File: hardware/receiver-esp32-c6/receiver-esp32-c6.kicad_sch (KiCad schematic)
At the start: 34 parts, among them J1 Conn_01x04, J2 Conn_01x04, J3 Conn_01x04, J4 Conn_01x06, J5 Conn_01x06, J6 Conn_01x02, J7 Conn_02x04_Counter_Clockwise, J8 Conn_02x03_Counter_Clockwise, J9 Conn_02x02_Counter_Clockwise, SW1 SW_Push_DPDT, U1 ESP32-C6-WROOM-1, U2 ULN2003, U3 MT3608, U4 MT3608

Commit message: First production version - with issues
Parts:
- removed J1, J2, J3: Conn_01x04, symbol Connector_Generic:Conn_01x04
- removed J9: Conn_02x02_Counter_Clockwise, symbol Connector_Generic:Conn_02x02_Counter_Clockwise
- added H1, H2, H3, H4: MountingHole, MountingHole:MountingHole_4mm_Pad_TopBottom, symbol Mechanical:MountingHole
- added J1, J11, J2, J3: Conn_01x03, Connector_PinHeader_2.54mm:PinHeader_1x03_P2.54mm_Vertical, symbol Connector_Generic:Conn_01x03
- added J10, J9: Conn_01x04, Connector_PinHeader_2.54mm:PinHeader_1x04_P2.54mm_Vertical, symbol Connector_Generic:Conn_01x04
- added R10, R11, R13, R14: 10kR 1%, Resistor_SMD:R_0603_1608Metric, symbol Device:R_US
- added R12: ???, Resistor_SMD:R_0805_2012Metric, symbol Device:R_US
- added SW2: SW_Push, Button_Switch_SMD:SW_SPST_PTS647_Sx38, symbol Switch:SW_Push
- added U5: INA226, Package_SO:VSSOP-10_3x3mm_P0.5mm, symbol Sensor_Energy:INA226
- C1, C2, C6, C7, C8, C9: footprint (none) -> Capacitor_SMD:C_0603_1608Metric
- D1, D4: footprint (none) -> Diode_SMD:D_SMF
- D3: footprint (none) -> LED_SMD:LED_0603_1608Metric
- J4, J5: footprint (none) -> Connector_PinHeader_2.54mm:PinHeader_1x06_P2.54mm_Vertical
- J6: footprint (none) -> Connector_JST:JST_EH_B2B-EH-A_1x02_P2.50mm_Vertical
- J7: footprint (none) -> Connector_IDC:IDC-Header_2x04_P2.54mm_Vertical
- J8: footprint (none) -> Connector_PinHeader_1.27mm:PinHeader_2x03_P1.27mm_Vertical_SMD
- L1, L2: footprint (none) -> Inductor_SMD:L_Changjiang_FNR5020S
- R1, R2, R3, R4, R5, R6, R7, R8, R9: footprint (none) -> Resistor_SMD:R_0603_1608Metric
- SW1: footprint (none) -> Minatel Library:Switch-6P-2way
- U2: footprint (none) -> Package_SO:SOP-16_3.9x9.9mm_P1.27mm
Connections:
- net +3V3: now also U1.2 (3V3), J9.1 (Pin_1), R10.2, R11.2, R13.1, R14.1, U5.6 (VS)
- net +5V: now also J1.2 (Pin_2), J11.2 (Pin_2), J2.2 (Pin_2), J3.2 (Pin_2)
- net BOOT: now also R14.2, SW2.2
- net GND: now also J1.3 (Pin_3), J10.4 (Pin_4), J11.3 (Pin_3), J2.3 (Pin_3), J3.3 (Pin_3), J9.4 (Pin_4), SW2.1, U5.1 (A1), U5.2 (A0), U5.7 (GND)
- net I2C_SCL: now also J9.2 (Pin_2), R11.1, U5.5 (SCL)
- net I2C_SDA: now also J9.3 (Pin_3), R10.1, U5.4 (SDA)
- net O_LED_1: now also U1.21 (GPIO23); no longer U1.16 (GPIO18)
- net O_LED_2: now also U1.20 (GPIO22); no longer U1.17 (GPIO19)
- net O_LED_3: now also U1.19 (GPIO21); no longer U1.18 (GPIO20)
- net O_LED_4: now also U1.18 (GPIO20); no longer U1.19 (GPIO21)
- net O_LED_5: now also U1.17 (GPIO19); no longer U1.20 (GPIO22)
- net O_LED_6: now also U1.16 (GPIO18); no longer U1.21 (GPIO23)
- net O_PWM_1: now also J1.1 (Pin_1)
- net O_PWM_2: now also J2.1 (Pin_1)
- net O_PWM_3: now also J3.1 (Pin_1)
- net O_PWM_4: now also J11.1 (Pin_1)
- net O_STEPPER_MS1: now also U1.23 (GPIO15)
- net USB_D+: now also J10.3 (Pin_3)
- net USB_D-: now also J10.2 (Pin_2)
- net VCC: now also J10.1 (Pin_1), R12.2, U5.9 (Vin-); no longer SW1.1 (A)
- net 3V3C: now reaches D4.2 (A), L2.2, U4.1 (SW)
- net 5VC: now reaches D1.2 (A), L1.2, U3.1 (SW)
- net VSS: now reaches SW1.4 (A)
- net VSS: now also SW1.1 (A), R12.1, U5.10 (Vin+), U5.8 (Vbus)
- new net: R13.2, U5.3 (~{Alert})
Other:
- company: (none) -> Pedro Minatel
- title: (none) -> ESP32-C6 ESP-NOW Receiver
- moved on the sheet: C8, C9, D3, J4, J5, J6, R3, R4, R9, SW1, U1, U2

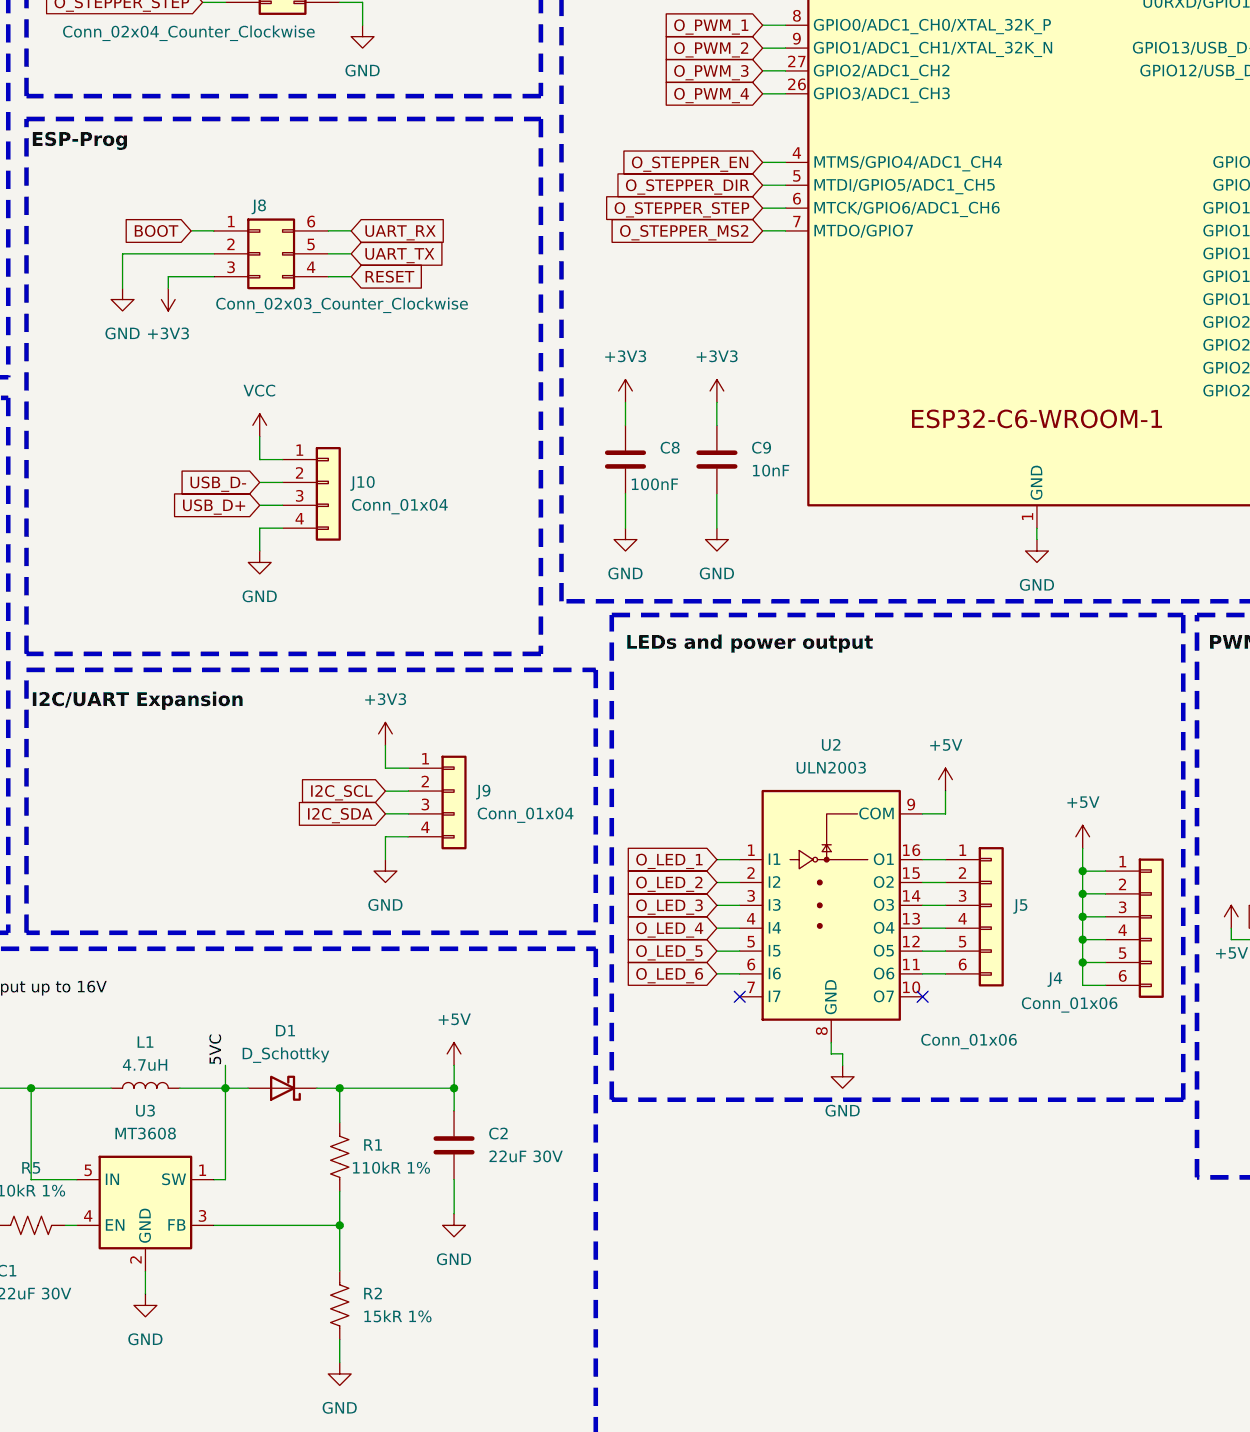
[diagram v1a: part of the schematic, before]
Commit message: Fixed the ESP-PROG pinout
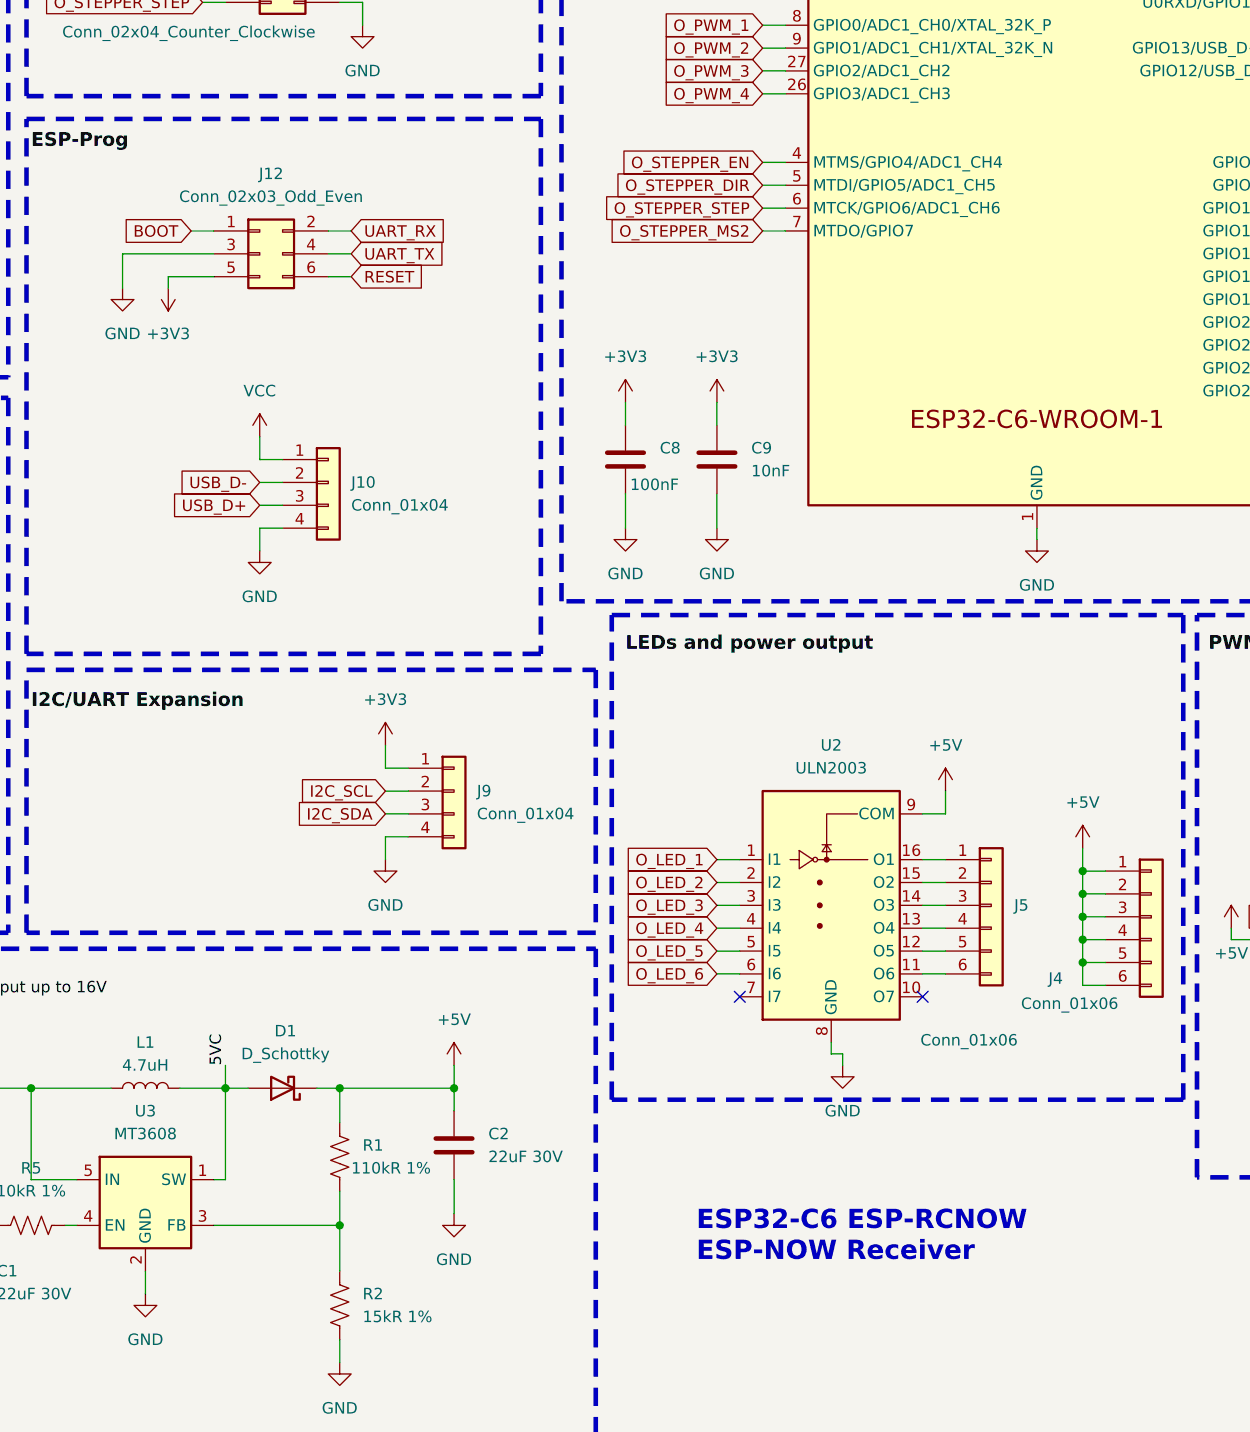
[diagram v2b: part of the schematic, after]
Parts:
- removed J8: Conn_02x03_Counter_Clockwise, Connector_PinHeader_1.27mm:PinHeader_2x03_P1.27mm_Vertical_SMD, symbol Connector_Generic:Conn_02x03_Counter_Clockwise
- added J12: Conn_02x03_Odd_Even, Connector_PinHeader_1.27mm:PinHeader_2x03_P1.27mm_Vertical_SMD, symbol Connector_Generic:Conn_02x03_Odd_Even
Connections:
- net +3V3: now also J12.5 (Pin_5)
- net BOOT: now also J12.1 (Pin_1)
- net GND: now also J12.3 (Pin_3)
- net RESET: now also J12.6 (Pin_6)
- net UART_RX: now also J12.2 (Pin_2)
- net UART_TX: now also J12.4 (Pin_4)
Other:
- note added: "ESP32-C6 ESP-RCNOW ESP-NOW Receiver"
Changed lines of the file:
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@@
 	(title_block
 		(title "ESP32-C6 ESP-NOW Receiver")
-		(date "2025-02-08")
-		(rev "1.0")
+		(date "2025-04-18")
+		(rev "2.0")
 		(company "Pedro Minatel")
 	)
@@
 		)
 	)
+	(text "ESP32-C6 ESP-RCNOW\nESP-NOW Receiver"
+		(exclude_from_sim no)
+		(at 178.054 171.45 0)
+		(effects
+			(font
+				(size 2.1336 2.1336)
+				(thickness 0.508)
+				(bold yes)
+			)
+			(justify left)
+		)
+	)
 	(junction
 		(at 63.5 154.94)
@@
 	)
 	(symbol
-		(lib_id "Connector_Generic:Conn_02x03_Counter_Clockwise")
-		(at 129.54 62.23 0)
-		(unit 1)
-		(exclude_from_sim no)
-		(in_bom yes)
-		(on_board yes)
-		(dnp no)
-		(property "Reference" "J8"
-			(at 129.54 56.896 0)
-			(effects
-				(font
-					(size 1.27 1.27)
-				)
-			)
-		)
-		(property "Value" "Conn_02x03_Counter_Clockwise"
-			(at 138.684 67.818 0)
-			(effects
-				(font
-					(size 1.27 1.27)
-				)
-			)
-		)
-		(property "Footprint" "Connector_PinHeader_1.27mm:PinHeader_2x03_P1.27mm_Vertical_SMD"
-			(at 129.54 62.23 0)
-			(effects
-				(font
-					(size 1.27 1.27)
-				)
-				(hide yes)
-			)
-		)
-		(property "Datasheet" "~"
-			(at 129.54 62.23 0)
-			(effects
-				(font
-					(size 1.27 1.27)
-				)
-				(hide yes)
-			)
-		)
-		(property "Description" "Generic connector, double row, 02x03, counter clockwise pin numbering scheme (similar to DIP package numbering), script generated (kicad-library-utils/schlib/autogen/connector/)"
-			(at 129.54 62.23 0)
-			(effects
-				(font
-					(size 1.27 1.27)
-				)
-				(hide yes)
-			)
-		)
-		(pin "1"
-		)
-		(pin "2"
-		)
-		(pin "3"
-		)
-		(pin "4"
-		)
-		(pin "5"
-		)
-		(pin "6"
-		)
-		(instances
-			(project ""
-				(path "/74785fdf-749b-4c5e-87ad-0cd9c1365ade"
-					(reference "J8")
-					(unit 1)
-				)
-			)
-		)
-	)
-	(symbol
 		(lib_id "Device:D_Schottky")
 		(at 57.15 154.94 180)
@@
 					(unit 1)
 				)
+			)
+		)
+	)
+	(symbol
+		(lib_id "Connector_Generic:Conn_02x03_Odd_Even")
+		(at 129.54 62.23 0)
+		(unit 1)
+		(exclude_from_sim no)
+		(in_bom yes)
+		(on_board yes)
+		(dnp no)
+		(fields_autoplaced yes)
+		(property "Reference" "J12"
+			(at 130.81 53.34 0)
+			(effects
+				(font
+					(size 1.27 1.27)
+				)
+			)
+		)
+		(property "Value" "Conn_02x03_Odd_Even"
+			(at 130.81 55.88 0)
+			(effects
+				(font
+					(size 1.27 1.27)
+				)
+			)
+		)
+		(property "Footprint" "Connector_PinHeader_1.27mm:PinHeader_2x03_P1.27mm_Vertical_SMD"
+			(at 129.54 62.23 0)
+			(effects
+				(font
+					(size 1.27 1.27)
+				)
+				(hide yes)
+			)
+		)
+		(property "Datasheet" "~"
+			(at 129.54 62.23 0)
+			(effects
+				(font
+					(size 1.27 1.27)
+				)
+				(hide yes)
+			)
+		)
+		(property "Description" "Generic connector, double row, 02x03, odd/even pin numbering scheme (row 1 odd numbers, row 2 even numbers), script generated (kicad-library-utils/schlib/autogen/connector/)"
+			(at 129.54 62.23 0)
+			(effects
+				(font
+					(size 1.27 1.27)
+				)
+				(hide yes)
+			)
+		)
+		(pin "1"
+		)
+		(pin "3"
+		)
+		(pin "5"
+		)
+		(pin "2"
+		)
+		(pin "4"
+		)
+		(pin "6"
+		)
+		(instances
+			(project ""
+				(path "/74785fdf-749b-4c5e-87ad-0cd9c1365ade"
+					(reference "J12")
+					(unit 1)
+				)
